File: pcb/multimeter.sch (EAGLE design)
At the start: 66 parts, among them IC1 AD822R, IC2 MEGA32-A, IC3 25C080SN, Q1 BSS123, Q2 BSS123, Q3 BSS123, Q4 BSS123

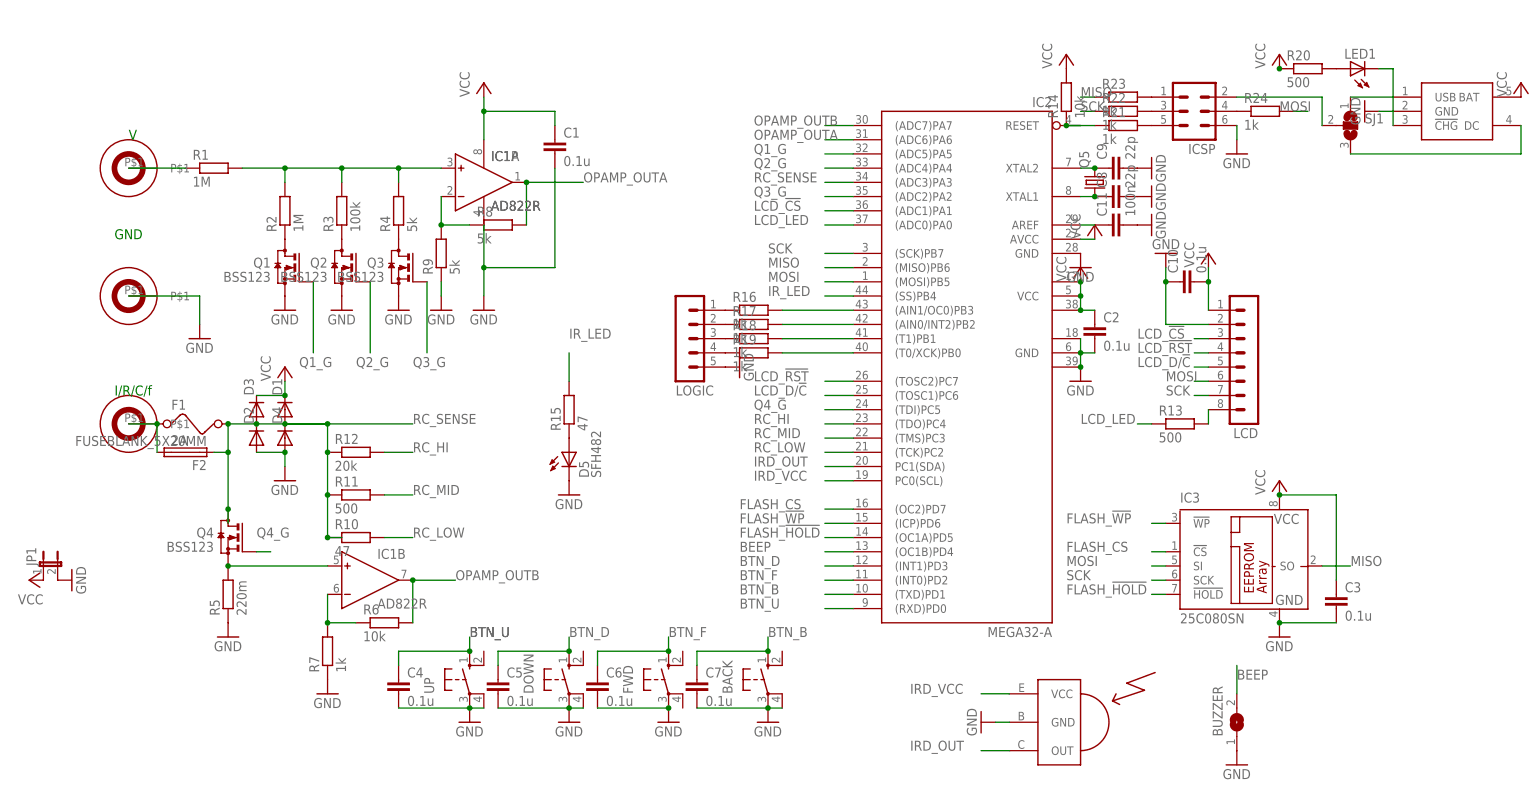
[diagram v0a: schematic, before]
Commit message: added pcb files, connected charge LED to DC input instead of battery, connected Flash VCC to same net as IRD VCC
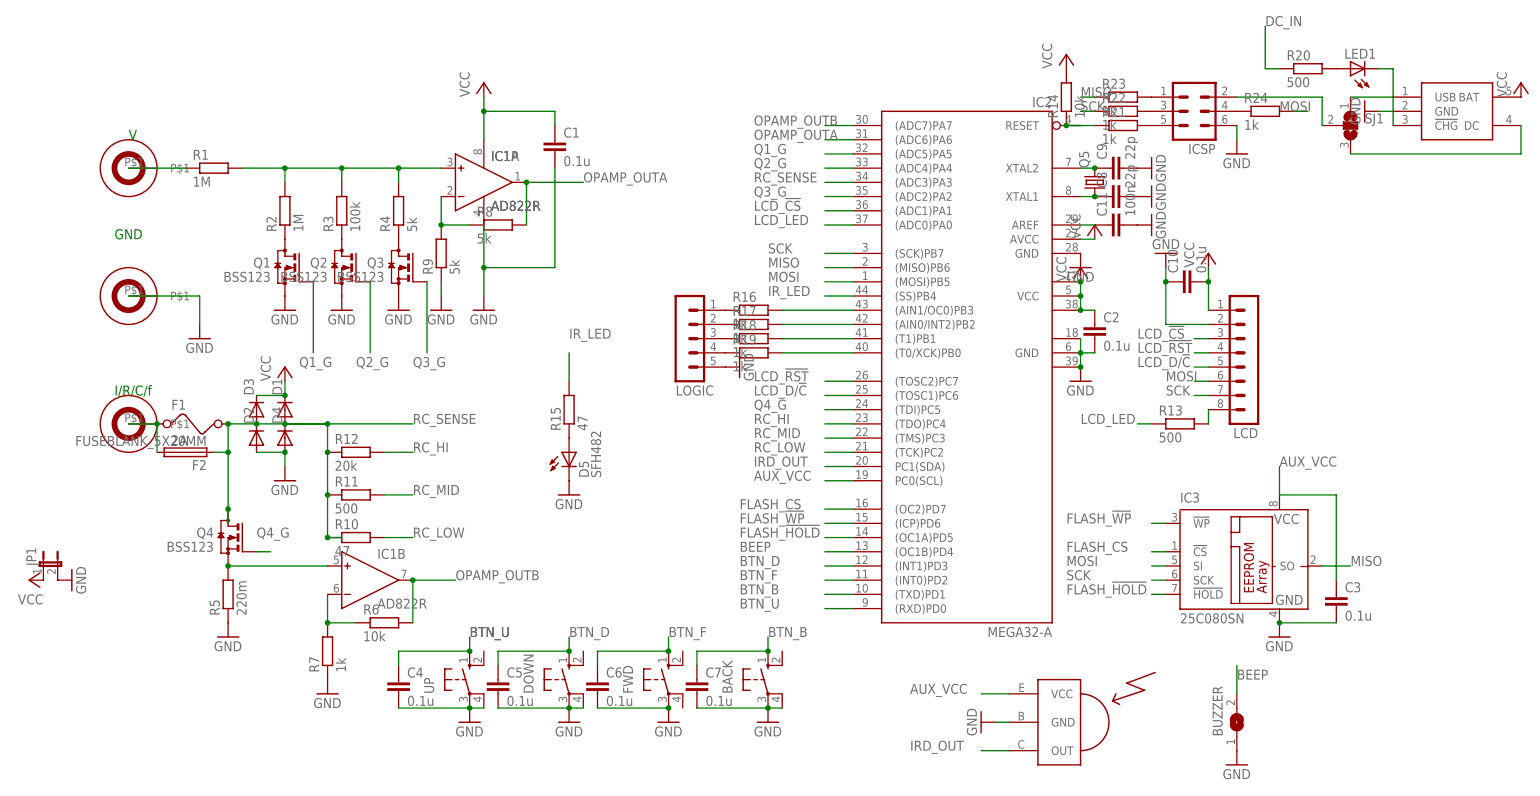
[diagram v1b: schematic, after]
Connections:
- removed net IRD_VCC: IC2.PC0(SCL), U$3.VCC
- removed net N$19: ICSP.2, SJ1.2
- new net AUX_VCC: C3.1, IC2.PC0(SCL), IC3.VCC, U$3.VCC
- new net DC_IN: ICSP.2, R20.1, SJ1.2
- net VCC: no longer C3.1, IC3.VCC, R20.1
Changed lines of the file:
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@@
 <part name="IC3" library="microchip" deviceset="25*" device="SN" technology="C080"/>
 <part name="GND11" library="supply1" deviceset="GND" device=""/>
-<part name="P+5" library="supply1" deviceset="VCC" device=""/>
 <part name="P+6" library="supply1" deviceset="VCC" device=""/>
 <part name="GND12" library="supply1" deviceset="GND" device=""/>
@@
 <part name="LED1" library="led" deviceset="LED" device="SML0805"/>
 <part name="R20" library="rcl" deviceset="R-EU_" device="R0805" value="500"/>
-<part name="P+10" library="supply1" deviceset="VCC" device=""/>
 <part name="R21" library="rcl" deviceset="R-EU_" device="R0805" value="1k"/>
 <part name="R22" library="rcl" deviceset="R-EU_" device="R0805" value="1k"/>
@@
 <instance part="IC3" gate="G$1" x="180.34" y="12.7"/>
 <instance part="GND11" gate="1" x="187.96" y="0"/>
-<instance part="P+5" gate="VCC" x="187.96" y="27.94"/>
 <instance part="P+6" gate="VCC" x="152.4" y="66.04"/>
 <instance part="GND12" gate="1" x="152.4" y="45.72"/>
@@
 <instance part="LED1" gate="G$1" x="200.66" y="101.6" rot="R90"/>
 <instance part="R20" gate="G$1" x="193.04" y="101.6"/>
-<instance part="P+10" gate="VCC" x="187.96" y="104.14"/>
 <instance part="R21" gate="G$1" x="160.02" y="91.44"/>
 <instance part="R22" gate="G$1" x="160.02" y="93.98"/>
@@
 </segment>
 <segment>
-<pinref part="IC3" gate="G$1" pin="VCC"/>
-<pinref part="P+5" gate="VCC" pin="VCC"/>
-<pinref part="C3" gate="G$1" pin="1"/>
-<wire x1="198.12" y1="10.16" x2="198.12" y2="25.4" width="0.1524" layer="91"/>
-<wire x1="198.12" y1="25.4" x2="187.96" y2="25.4" width="0.1524" layer="91"/>
-<junction x="187.96" y="25.4"/>
-</segment>
-<segment>
 <pinref part="IC2" gate="G$1" pin="VCC2"/>
 <pinref part="IC2" gate="G$1" pin="VCC"/>
@@
 <pinref part="U$4" gate="G$1" pin="BAT"/>
 <pinref part="P+3" gate="VCC" pin="VCC"/>
-</segment>
-<segment>
-<pinref part="R20" gate="G$1" pin="1"/>
-<pinref part="P+10" gate="VCC" pin="VCC"/>
-<pinref part="P+10" gate="VCC" pin="VCC"/>
-<junction x="187.96" y="101.6"/>
 </segment>
 </net>
@@
 </segment>
 </net>
-<net name="IRD_VCC" class="0">
-<segment>
-<pinref part="U$3" gate="G$1" pin="VCC"/>
-<wire x1="139.7" y1="-10.16" x2="134.62" y2="-10.16" width="0.1524" layer="91"/>
-<label x="121.92" y="-10.16" size="1.778" layer="95"/>
-</segment>
-<segment>
-<pinref part="IC2" gate="G$1" pin="PC0(SCL)"/>
-<wire x1="111.76" y1="27.94" x2="106.68" y2="27.94" width="0.1524" layer="91"/>
-<label x="93.98" y="27.94" size="1.778" layer="95"/>
-</segment>
-</net>
 <net name="N$1" class="0">
 <segment>
@@
 </segment>
 </net>
-<net name="N$19" class="0">
+<net name="DC_IN" class="0">
 <segment>
 <pinref part="ICSP" gate="1" pin="2"/>
@@
 <wire x1="195.58" y1="96.52" x2="195.58" y2="91.44" width="0.1524" layer="91"/>
 </segment>
+<segment>
+<pinref part="R20" gate="G$1" pin="1"/>
+<wire x1="187.96" y1="101.6" x2="185.42" y2="101.6" width="0.1524" layer="91"/>
+<wire x1="185.42" y1="101.6" x2="185.42" y2="109.22" width="0.1524" layer="91"/>
+<label x="185.42" y="109.22" size="1.778" layer="95"/>
+</segment>
 </net>
 <net name="N$20" class="0">
@@
 </segment>
 </net>
+<net name="AUX_VCC" class="0">
+<segment>
+<pinref part="IC2" gate="G$1" pin="PC0(SCL)"/>
+<wire x1="111.76" y1="27.94" x2="106.68" y2="27.94" width="0.1524" layer="91"/>
+<label x="93.98" y="27.94" size="1.778" layer="95"/>
+</segment>
+<segment>
+<pinref part="IC3" gate="G$1" pin="VCC"/>
+<pinref part="C3" gate="G$1" pin="1"/>
+<wire x1="198.12" y1="10.16" x2="198.12" y2="25.4" width="0.1524" layer="91"/>
+<wire x1="198.12" y1="25.4" x2="187.96" y2="25.4" width="0.1524" layer="91"/>
+<label x="187.96" y="30.48" size="1.778" layer="95"/>
+<wire x1="187.96" y1="25.4" x2="187.96" y2="30.48" width="0.1524" layer="91"/>
+</segment>
+<segment>
+<pinref part="U$3" gate="G$1" pin="VCC"/>
+<wire x1="139.7" y1="-10.16" x2="134.62" y2="-10.16" width="0.1524" layer="91"/>
+<label x="121.92" y="-10.16" size="1.778" layer="95"/>
+</segment>
+</net>
